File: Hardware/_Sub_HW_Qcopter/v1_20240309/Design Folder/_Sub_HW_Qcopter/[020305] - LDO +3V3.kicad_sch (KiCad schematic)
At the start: 6 parts, among them U3601 TLV74033PDBVR

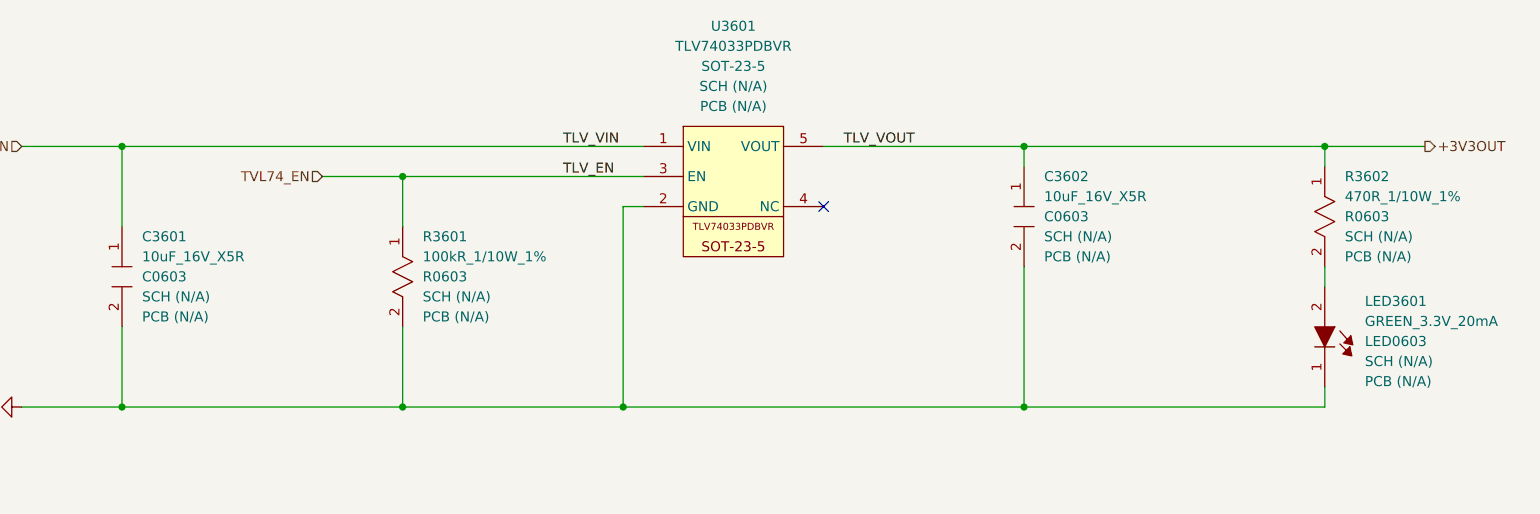
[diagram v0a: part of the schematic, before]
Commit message: Update [020305] - LDO +3V3.kicad_sch
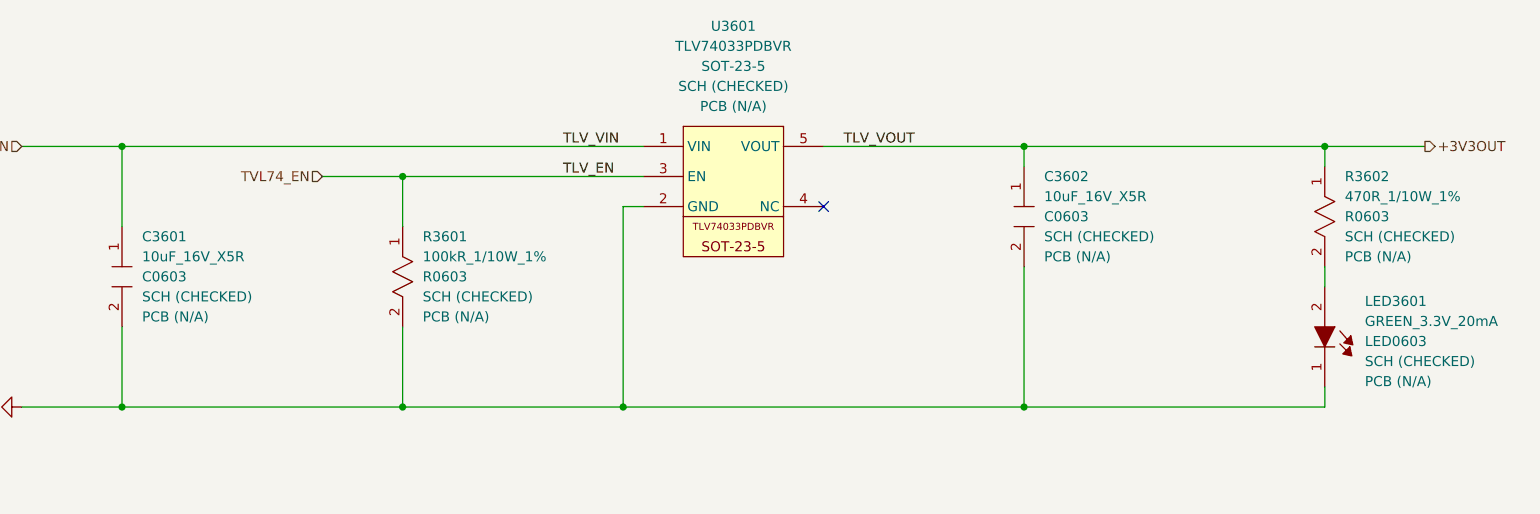
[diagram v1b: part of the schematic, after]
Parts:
- C3601, C3602, LED3601, R3601, R3602, U3601: SCH CHECK SCH (N/A) -> SCH (CHECKED)
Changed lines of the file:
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@@
 			)
 		)
-		(property "SCH CHECK" "SCH (N/A)"
+		(property "SCH CHECK" "SCH (CHECKED)"
 			(at 294.64 204.4699 90)
 			(effects
@@
 			)
 		)
-		(property "SCH CHECK" "SCH (N/A)"
+		(property "SCH CHECK" "SCH (CHECKED)"
 			(at 332.74 204.4699 90)
 			(effects
@@
 			)
 		)
-		(property "SCH CHECK" "SCH (N/A)"
+		(property "SCH CHECK" "SCH (CHECKED)"
 			(at 215.9 212.0899 90)
 			(effects
@@
 			)
 		)
-		(property "SCH CHECK" "SCH (N/A)"
+		(property "SCH CHECK" "SCH (CHECKED)"
 			(at 255.27 185.42 0)
 			(effects
@@
 			)
 		)
-		(property "SCH CHECK" "SCH (N/A)"
+		(property "SCH CHECK" "SCH (CHECKED)"
 			(at 180.34 212.0899 90)
 			(effects
@@
 			)
 		)
-		(property "SCH CHECK" "SCH (N/A)"
+		(property "SCH CHECK" "SCH (CHECKED)"
 			(at 335.28 220.2814 90)
 			(effects
